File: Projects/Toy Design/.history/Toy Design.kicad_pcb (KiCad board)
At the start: 2 copper layers, 100 x 114.5 mm, 78 parts, among them J1 Conn_01x01_Pin, J2 Conn_01x01_Pin, U1 TLV61048DBVR, U10 STM32G030K6T6, U11 MCP3208-CI/SL, U12 74HC595, U13 74HC595, U14 74HC595, U15 74HC595, U16 74HC595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

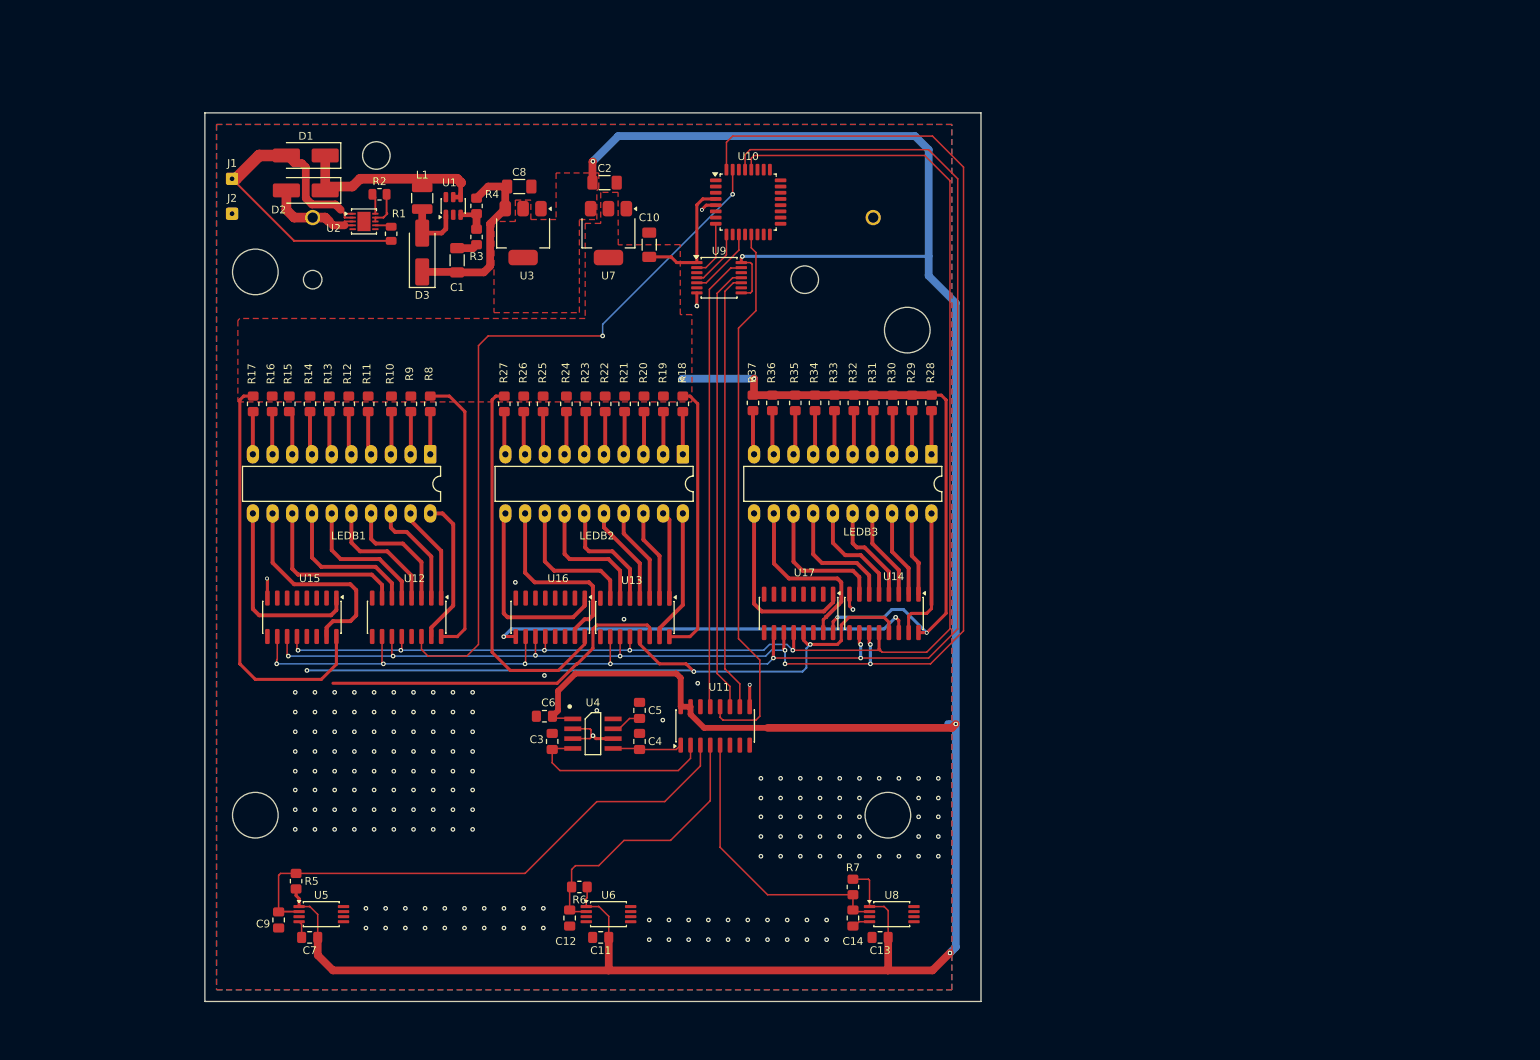
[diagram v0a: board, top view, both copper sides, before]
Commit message: Updated PCB edge to be inline with the design ifile in CLaude
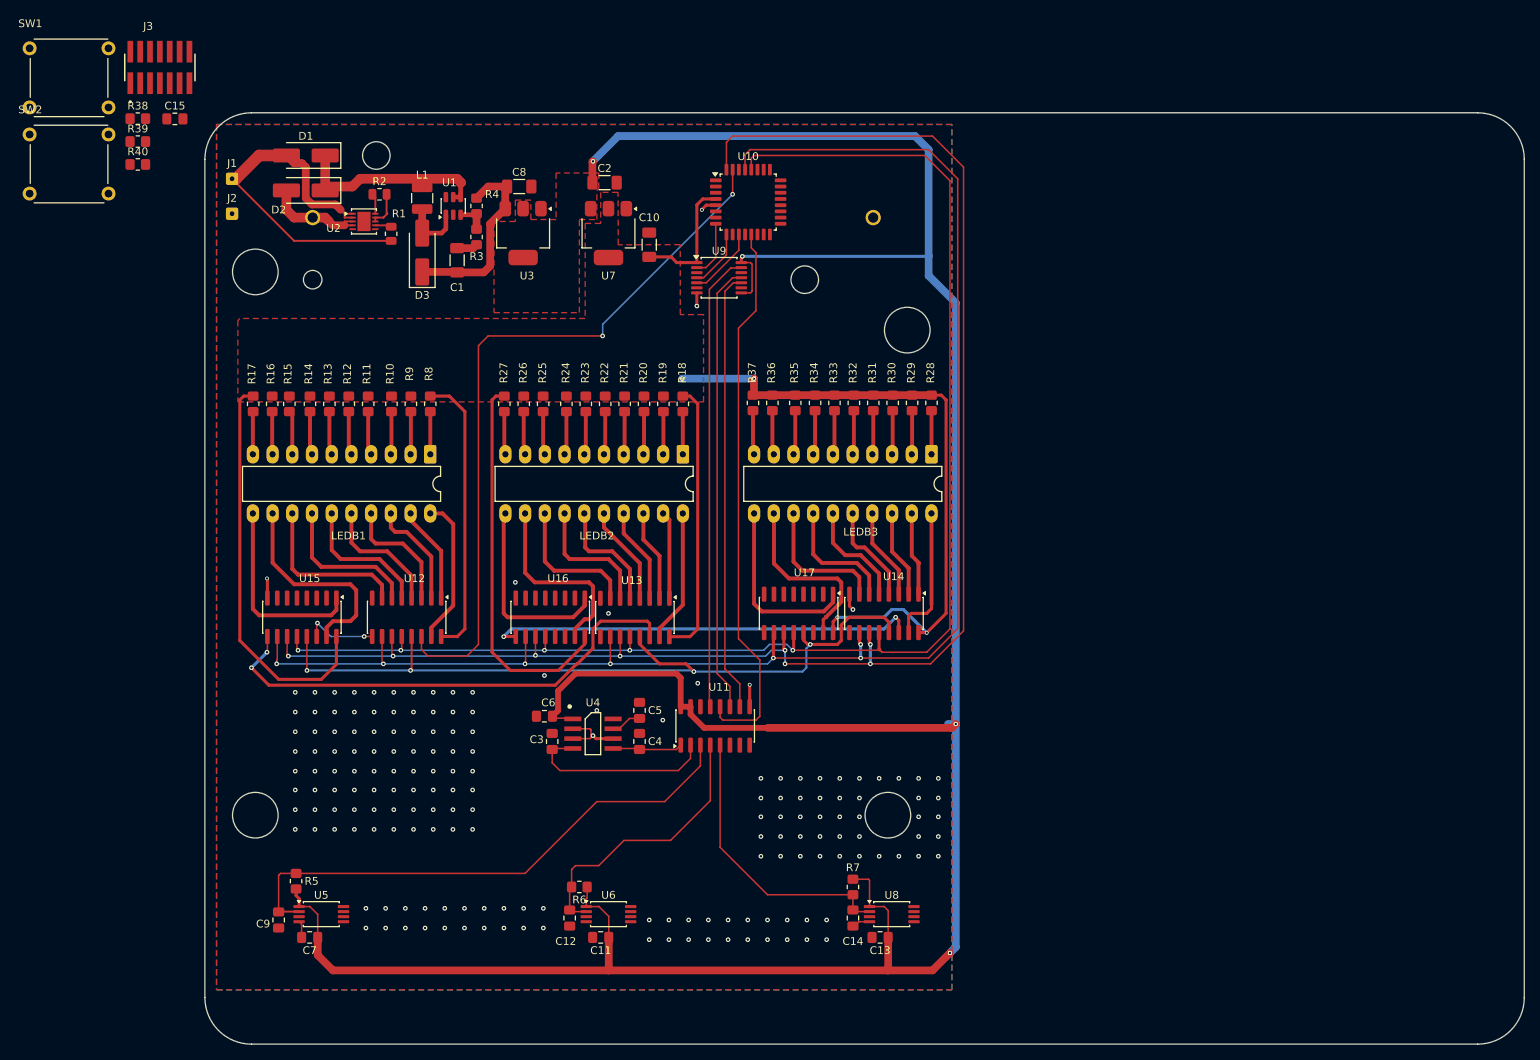
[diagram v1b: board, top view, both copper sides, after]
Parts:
- added C15: 100nF, Capacitor_SMD:C_0805_2012Metric_Pad1.18x1.45mm_HandSolder, F.Cu at (92.6, 32.3)
- added J3: FTSH-107-01-X-DV-K-TR, ToyDesign:SAMTEC_FTSH-107-01-X-DV-K-TR, F.Cu at (90.7, 25.7)
- added R38: 100k, Resistor_SMD:R_0805_2012Metric_Pad1.20x1.40mm_HandSolder, F.Cu at (87.9, 32.3)
- added R39: 100k, Resistor_SMD:R_0805_2012Metric_Pad1.20x1.40mm_HandSolder, F.Cu at (87.9, 35.2)
- added R40: 100k, Resistor_SMD:R_0805_2012Metric_Pad1.20x1.40mm_HandSolder, F.Cu at (87.9, 38.2)
- added SW1: 5GTH935, ToyDesign:5GTH9, F.Cu at (79.0, 27.0)
- added SW2: 5GTH935, ToyDesign:5GTH9, F.Cu at (79.0, 38.1)
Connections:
- U10 pad 15: unconnected-(U10-PB0-Pad15) -> Net-(U10-PB0)
- U10 pad 16: unconnected-(U10-PB1-Pad16) -> Net-(U10-PB1)
- U10 pad 24: unconnected-(U10-PA13-Pad24) -> SWDIO
- U10 pad 25: unconnected-(U10-PA14-Pad25) -> SWCLK
- U10 pad 6: unconnected-(U10-NRST-Pad6) -> NRST
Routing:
- net Net-(U13-SER): track 46.7 -> 63.8 mm, vias 0 -> 2
- net Net-(U12-QH'): track 0.00 -> 9.57 mm, vias 0 -> 2
- net ~{OE}: track 93.6 -> 102.6 mm, vias 3 -> 4
- net +3.3V: track 276.0 -> 274.3 mm
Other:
- board size 100 x 114.5 mm -> 170 x 120 mm
